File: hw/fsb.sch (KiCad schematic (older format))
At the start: 5 parts, among them J101 AMPSEAL_8_POS_VERT_WHITE_SEAL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, J102 AMPSEAL_23_POS_VERT_WHITE_SEA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

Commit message: creating hw 3.0.0
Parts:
- removed R101: 10K, multicomp:0603, symbol 10K
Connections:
- net labels added: AUX_15A, HEATER_15+, HEATER_15-, HORN_4A, RADIO_4A
- net labels removed: AUX_10A, HEATER_15A+, HEATER_15A-, HORN_5A, RADIO_2A
- wire segments 76 -> 64

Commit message: key_50 moved out from ISP pin
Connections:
- wire segments 64 -> 67

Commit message: radio & aux are on when ign key is on
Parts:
- added R101, R102, R103, R104: 1K, yageo:0603, symbol 1K
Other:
- moved on the sheet: F102

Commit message: heater shuts down when ignition key is turned off
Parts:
- J101: symbol AMPSEAL_8_POS_VERT_WHITE_SEALED_1-776276-2 -> AMPSEAL_8_POS_VERT_WHITE_SEALED_1-776276-2-RESCUE-fsb
- J102: symbol AMPSEAL_23_POS_VERT_WHITE_SEALED_1-776228-2 -> AMPSEAL_23_POS_VERT_WHITE_SEALED_1-776228-2-RESCUE-fsb
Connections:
- net labels added: GND, UI_4A
- net labels removed: HEATER_15-
- wire segments 67 -> 73

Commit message: hw 2.1.0 created, not yet ordered
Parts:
- added R105, R106: 1K, yageo:0603, symbol 1K
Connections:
- net HORN_4A: now also J102.P$18 (S); no longer J102.P$19 (S)
- net RADIO_4A: now also J102.P$10 (S); no longer J102.P$18 (S)
- net at J102.P$6 (S): now also R105.2 (R2)
- net at J102.P$7 (S): now also R106.2 (R2)
- new net LPC1549/DOORSW1: R105.1 (R1)
- new net LPC1549/DOORSW2: R106.1 (R1)
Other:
- note added: "Door switches,\nfor example Omron D3D-111"
- moved on the sheet: J102F, J102G, J102J, J102R, J102S
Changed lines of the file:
@@
 F18 "UI" O R 6400 4600 60
 F19 "UI_SENSE" I R 6400 4700 60
+F20 "DOORSW1" I L 4250 4900 60
+F21 "DOORSW2" I L 4250 5050 60
 $EndSheet
 $Comp
@@
 L AMPSEAL_23_POS_VERT_WHITE_SEALED_1-776228-2-RESCUE-fsb J102
 U 6 1 5988B296
-P 10900 2950
-F 0 "J102" H 10868 3033 45  0000 C CNN
-F 1 "AMPSEAL_23_POS_VERT_WHITE_SEALED_1-776228-2" H 10900 2950 45  0001 L BNN
-F 2 "usevolt:AMPSEAL_23_POS_776200-1" H 10930 3100 20  0001 C CNN
-F 3 "http://www.mouser.com/ds/2/418/NG_CD_776228_C13-692101.pdf" H 11000 2920 60  0001 C CNN
-F 4 "571-1-776228-2" H 11400 3320 60  0001 C CNN "1st Source Part Number"
-F 5 "1-776228-2" H 11200 3120 60  0001 C CNN "Manufacturer Part Number"
-F 6 "Mouser" H 11300 3220 60  0001 C CNN "1st Source"
-F 7 "TE Connectivity" H 11100 3020 60  0001 C CNN "Manufacturer"
-	6    10900 2950
-	1    0    0    -1
+P 3150 4900
+F 0 "J102" H 3118 4983 45  0000 C CNN
+F 1 "AMPSEAL_23_POS_VERT_WHITE_SEALED_1-776228-2" H 3150 4900 45  0001 L BNN
+F 2 "usevolt:AMPSEAL_23_POS_776200-1" H 3180 5050 20  0001 C CNN
+F 3 "http://www.mouser.com/ds/2/418/NG_CD_776228_C13-692101.pdf" H 3250 4870 60  0001 C CNN
+F 4 "571-1-776228-2" H 3650 5270 60  0001 C CNN "1st Source Part Number"
+F 5 "1-776228-2" H 3450 5070 60  0001 C CNN "Manufacturer Part Number"
+F 6 "Mouser" H 3550 5170 60  0001 C CNN "1st Source"
+F 7 "TE Connectivity" H 3350 4970 60  0001 C CNN "Manufacturer"
+	6    3150 4900
+	-1   0    0    -1
 $EndComp
 $Comp
 L AMPSEAL_23_POS_VERT_WHITE_SEALED_1-776228-2-RESCUE-fsb J102
 U 7 1 5988B310
-P 10900 3100
-F 0 "J102" H 10868 3183 45  0000 C CNN
-F 1 "AMPSEAL_23_POS_VERT_WHITE_SEALED_1-776228-2" H 10900 3100 45  0001 L BNN
-F 2 "usevolt:AMPSEAL_23_POS_776200-1" H 10930 3250 20  0001 C CNN
-F 3 "http://www.mouser.com/ds/2/418/NG_CD_776228_C13-692101.pdf" H 11000 3070 60  0001 C CNN
-F 4 "571-1-776228-2" H 11400 3470 60  0001 C CNN "1st Source Part Number"
-F 5 "1-776228-2" H 11200 3270 60  0001 C CNN "Manufacturer Part Number"
-F 6 "Mouser" H 11300 3370 60  0001 C CNN "1st Source"
-F 7 "TE Connectivity" H 11100 3170 60  0001 C CNN "Manufacturer"
-	7    10900 3100
-	1    0    0    -1
+P 3150 5050
+F 0 "J102" H 3118 5133 45  0000 C CNN
+F 1 "AMPSEAL_23_POS_VERT_WHITE_SEALED_1-776228-2" H 3150 5050 45  0001 L BNN
+F 2 "usevolt:AMPSEAL_23_POS_776200-1" H 3180 5200 20  0001 C CNN
+F 3 "http://www.mouser.com/ds/2/418/NG_CD_776228_C13-692101.pdf" H 3250 5020 60  0001 C CNN
+F 4 "571-1-776228-2" H 3650 5420 60  0001 C CNN "1st Source Part Number"
+F 5 "1-776228-2" H 3450 5220 60  0001 C CNN "Manufacturer Part Number"
+F 6 "Mouser" H 3550 5320 60  0001 C CNN "1st Source"
+F 7 "TE Connectivity" H 3350 5120 60  0001 C CNN "Manufacturer"
+	7    3150 5050
+	-1   0    0    -1
 $EndComp
 $Comp
@@
 L AMPSEAL_23_POS_VERT_WHITE_SEALED_1-776228-2-RESCUE-fsb J102
 U 10 1 5988B48A
-P 10900 3550
-F 0 "J102" H 10868 3633 45  0000 C CNN
-F 1 "AMPSEAL_23_POS_VERT_WHITE_SEALED_1-776228-2" H 10900 3550 45  0001 L BNN
-F 2 "usevolt:AMPSEAL_23_POS_776200-1" H 10930 3700 20  0001 C CNN
-F 3 "http://www.mouser.com/ds/2/418/NG_CD_776228_C13-692101.pdf" H 11000 3520 60  0001 C CNN
-F 4 "571-1-776228-2" H 11400 3920 60  0001 C CNN "1st Source Part Number"
-F 5 "1-776228-2" H 11200 3720 60  0001 C CNN "Manufacturer Part Number"
-F 6 "Mouser" H 11300 3820 60  0001 C CNN "1st Source"
-F 7 "TE Connectivity" H 11100 3620 60  0001 C CNN "Manufacturer"
-	10   10900 3550
+P 10350 3700
+F 0 "J102" H 10318 3783 45  0000 C CNN
+F 1 "AMPSEAL_23_POS_VERT_WHITE_SEALED_1-776228-2" H 10350 3700 45  0001 L BNN
+F 2 "usevolt:AMPSEAL_23_POS_776200-1" H 10380 3850 20  0001 C CNN
+F 3 "http://www.mouser.com/ds/2/418/NG_CD_776228_C13-692101.pdf" H 10450 3670 60  0001 C CNN
+F 4 "571-1-776228-2" H 10850 4070 60  0001 C CNN "1st Source Part Number"
+F 5 "1-776228-2" H 10650 3870 60  0001 C CNN "Manufacturer Part Number"
+F 6 "Mouser" H 10750 3970 60  0001 C CNN "1st Source"
+F 7 "TE Connectivity" H 10550 3770 60  0001 C CNN "Manufacturer"
+	10   10350 3700
 	1    0    0    -1
 $EndComp
@@
 L AMPSEAL_23_POS_VERT_WHITE_SEALED_1-776228-2-RESCUE-fsb J102
 U 18 1 5988B8D6
-P 10350 3700
-F 0 "J102" H 10318 3783 45  0000 C CNN
-F 1 "AMPSEAL_23_POS_VERT_WHITE_SEALED_1-776228-2" H 10350 3700 45  0001 L BNN
-F 2 "usevolt:AMPSEAL_23_POS_776200-1" H 10380 3850 20  0001 C CNN
-F 3 "http://www.mouser.com/ds/2/418/NG_CD_776228_C13-692101.pdf" H 10450 3670 60  0001 C CNN
-F 4 "571-1-776228-2" H 10850 4070 60  0001 C CNN "1st Source Part Number"
-F 5 "1-776228-2" H 10650 3870 60  0001 C CNN "Manufacturer Part Number"
-F 6 "Mouser" H 10750 3970 60  0001 C CNN "1st Source"
-F 7 "TE Connectivity" H 10550 3770 60  0001 C CNN "Manufacturer"
-	18   10350 3700
-	1    0    0    -1
-$EndComp
-$Comp
-L AMPSEAL_23_POS_VERT_WHITE_SEALED_1-776228-2-RESCUE-fsb J102
-U 19 1 5988C267
 P 10150 3600
 F 0 "J102" H 10118 3683 45  0000 C CNN
@@
 F 6 "Mouser" H 10550 3870 60  0001 C CNN "1st Source"
 F 7 "TE Connectivity" H 10350 3670 60  0001 C CNN "Manufacturer"
-	19   10150 3600
+	18   10150 3600
+	1    0    0    -1
+$EndComp
+$Comp
+L AMPSEAL_23_POS_VERT_WHITE_SEALED_1-776228-2-RESCUE-fsb J102
+U 19 1 5988C267
+P 10900 3700
+F 0 "J102" H 10868 3783 45  0000 C CNN
+F 1 "AMPSEAL_23_POS_VERT_WHITE_SEALED_1-776228-2" H 10900 3700 45  0001 L BNN
+F 2 "usevolt:AMPSEAL_23_POS_776200-1" H 10930 3850 20  0001 C CNN
+F 3 "http://www.mouser.com/ds/2/418/NG_CD_776228_C13-692101.pdf" H 11000 3670 60  0001 C CNN
+F 4 "571-1-776228-2" H 11400 4070 60  0001 C CNN "1st Source Part Number"
+F 5 "1-776228-2" H 11200 3870 60  0001 C CNN "Manufacturer Part Number"
+F 6 "Mouser" H 11300 3970 60  0001 C CNN "1st Source"
+F 7 "TE Connectivity" H 11100 3770 60  0001 C CNN "Manufacturer"
+	19   10900 3700
 	1    0    0    -1
 $EndComp
@@
 Wire Wire Line
 	7300 4700 6400 4700
+Wire Wire Line
+	4250 5050 3750 5050
+Wire Wire Line
+	3750 4900 4250 4900
+$Comp
+L 1K R105
+U 1 1 5A09BE6F
+P 3550 4900
+F 0 "R105" H 3600 5084 45  0000 C CNN
+F 1 "1K" H 3600 5000 45  0000 C CNN
+F 2 "yageo:0603" H 3580 5050 20  0001 C CNN
+F 3 "" H 3519 4939 60  0001 C CNN
+F 4 "" H 3919 5339 60  0001 C CNN "1st Source Part Number"
+F 5 "Digikey" H 3819 5239 60  0001 C CNN "1st Source"
+F 6 "RC0603FR-071KL" H 3719 5139 60  0001 C CNN "Manufacturer Part Number"
+F 7 "YAGEO" H 3619 5039 60  0001 C CNN "Manufacturer"
+	1    3550 4900
+	1    0    0    -1
+$EndComp
+$Comp
+L 1K R106
+U 1 1 5A09C192
+P 3550 5050
+F 0 "R106" H 3600 5234 45  0000 C CNN
+F 1 "1K" H 3600 5150 45  0000 C CNN
+F 2 "yageo:0603" H 3580 5200 20  0001 C CNN
+F 3 "" H 3519 5089 60  0001 C CNN
+F 4 "" H 3919 5489 60  0001 C CNN "1st Source Part Number"
+F 5 "Digikey" H 3819 5389 60  0001 C CNN "1st Source"
+F 6 "RC0603FR-071KL" H 3719 5289 60  0001 C CNN "Manufacturer Part Number"
+F 7 "YAGEO" H 3619 5189 60  0001 C CNN "Manufacturer"
+	1    3550 5050
+	1    0    0    -1
+$EndComp
+Wire Wire Line
+	3450 4900 3250 4900
+Wire Wire Line
+	3250 5050 3450 5050
+Text Notes 1650 5050 0    60   ~ 0
+Door switches,\nfor example Omron D3D-111
 $EndSCHEMATC

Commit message: making 2.2.0 pcb
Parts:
- added R107: 1K, yageo:0603, symbol 1K
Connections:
- net at J102.P$8 (S): now also R107.2 (R2)
- new net LPC1549/SEATSW: R107.1 (R1)
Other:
- moved on the sheet: J102H, J102J, J102L, J102M, J102N, J102O, J102R, J102T, J102W

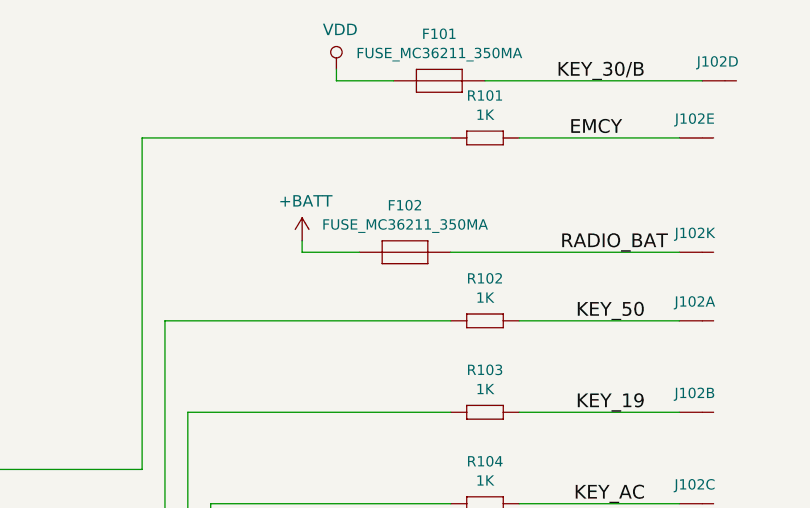
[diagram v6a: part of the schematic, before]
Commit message: radio fuse changed to 750 mA one
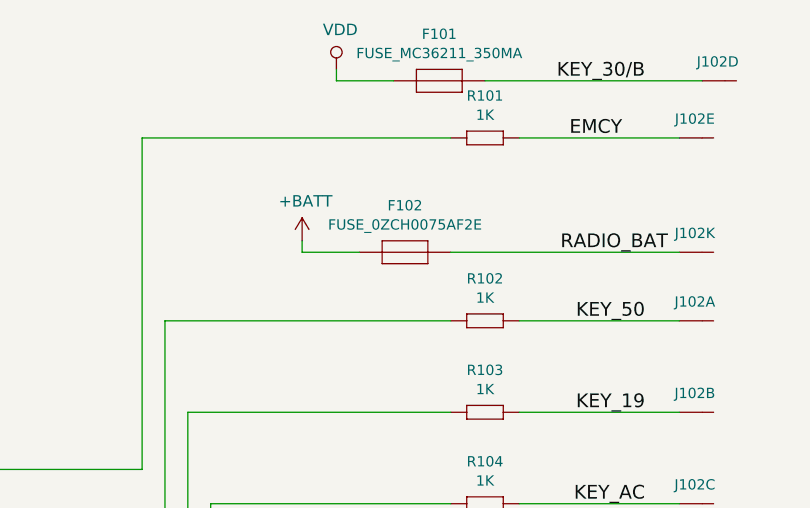
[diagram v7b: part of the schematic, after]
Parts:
- removed F102: FUSE_MC36211_350MA, usevolt:FUSE_MC36211, symbol FUSE_MC36211_350MA
- added F102: FUSE_0ZCH0075AF2E, usevolt:1210, symbol FUSE_0ZCH0075AF2E
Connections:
- net +BATT: now also F102.1
- net RADIO_BAT: now also F102.2
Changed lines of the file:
@@
-	1    0    0    -1
-$EndComp
-$Comp
-L FUSE_MC36211_350MA F102
-U 1 1 598F0936
-P 8800 1950
-F 0 "F102" H 8800 2154 45  0000 C CNN
-F 1 "FUSE_MC36211_350MA" H 8800 2070 45  0000 C CNN
-F 2 "usevolt:FUSE_MC36211" H 8830 2100 20  0001 C CNN
-F 3 "http://www.farnell.com/datasheets/1678471.pdf?_ga=1.218604761.1948984246.1460023966" H 8920 1970 60  0001 C CNN
-F 4 "Farnell" H 9220 2270 60  0001 C CNN "1st Source"
-F 5 "MC36211" H 9120 2170 60  0001 C CNN "Manufacturer Part Number"
-F 6 "MC36211" H 9320 2370 60  0001 C CNN "1st Source Part Number"
-F 7 "Multicomp" H 9020 2070 60  0001 C CNN "Manufacturer"
-	1    8800 1950
 	1    0    0    -1
 $EndComp
@@
 F4 "SENSE1" O L 8500 5100 60
 $EndSheet
+$Comp
+L FUSE_0ZCH0075AF2E F102
+U 1 1 5A8A8B03
+P 8800 1950
+F 0 "F102" H 8800 2154 45  0000 C CNN
+F 1 "FUSE_0ZCH0075AF2E" H 8800 2070 45  0000 C CNN
+F 2 "usevolt:1210" H 8830 2100 20  0001 C CNN
+F 3 "https://belfuse.com/resources/CircuitProtection/datasheets/0ZCH%20Nov2016.pdf" H 8920 1970 60  0001 C CNN
+F 4 "507-1788-1-ND" H 9320 2370 60  0001 C CNN "1st Source Part Number"
+F 5 "Digikey" H 9220 2270 60  0001 C CNN "1st Source"
+F 6 "0ZCH0075AF2E" H 9120 2170 60  0001 C CNN "Manufacturer Part Number"
+F 7 "Bel Fuse Inc." H 9020 2070 60  0001 C CNN "Manufacturer"
+	1    8800 1950
+	1    0    0    -1
+$EndComp
 $EndSCHEMATC

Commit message: 3.0.0 hw with low side heater mosfet
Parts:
- F101: symbol FUSE_MC36211_350MA -> fsb-rescue:FUSE_MC36211_350MA
- F102: symbol FUSE_0ZCH0075AF2E -> fsb-rescue:FUSE_0ZCH0075AF2E
- J101: symbol AMPSEAL_8_POS_VERT_WHITE_SEALED_1-776276-2-RESCUE-fsb -> fsb-rescue:AMPSEAL_8_POS_VERT_WHITE_SEALED_1-776276-2-RESCUE-fsb
- J102: symbol AMPSEAL_23_POS_VERT_WHITE_SEALED_1-776228-2-RESCUE-fsb -> fsb-rescue:AMPSEAL_23_POS_VERT_WHITE_SEALED_1-776228-2-RESCUE-fsb
- R101, R102, R103, R104, R105, R106, R107: symbol 1K -> fsb-rescue:1K
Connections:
- net HEATER_15-: now reaches J102.P$22 (S)
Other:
- moved on the sheet: J102V
